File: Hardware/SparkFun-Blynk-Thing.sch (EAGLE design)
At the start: 103 parts, among them IC1 LMV358, Q1 2.5A/30V, Q2 MMBT2222A, Q3 MMBT2222A, U1 MCP73831, U2 ESP8266, U3 AP2112K-3.3V, U4 FT231XS-U, U5 W25Q32FVSS, U6 SI7021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

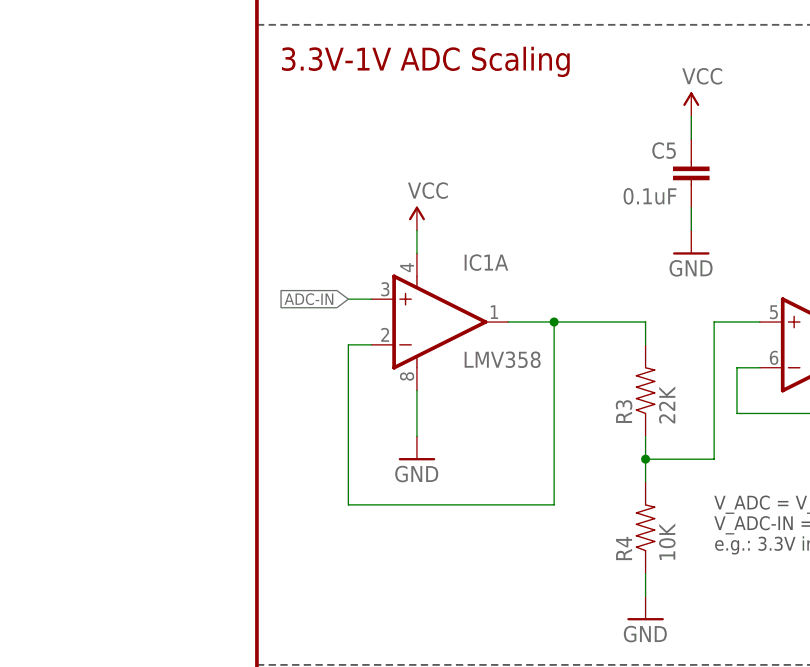
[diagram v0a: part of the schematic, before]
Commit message: Fixing Op amp power supply.
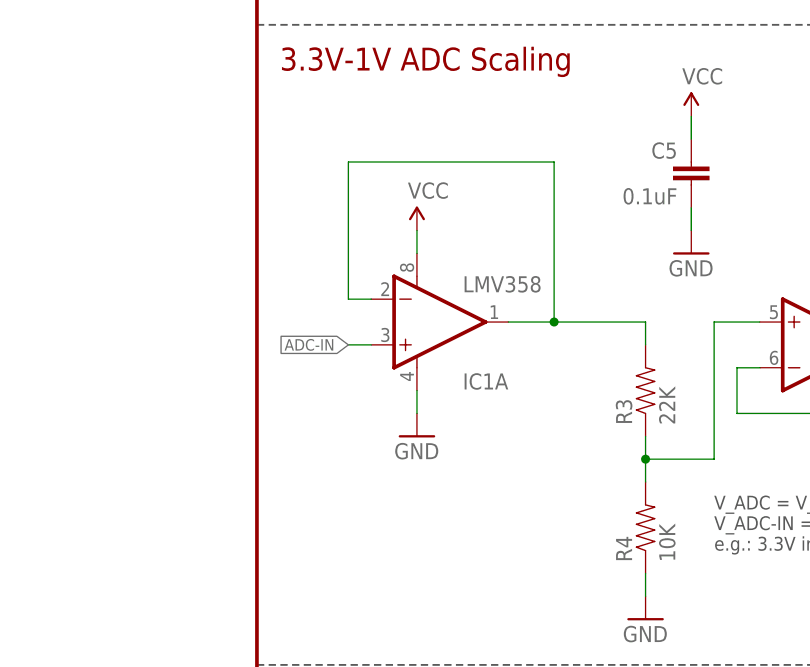
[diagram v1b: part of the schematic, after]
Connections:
- net GND: now also IC1A.V-; no longer IC1A.V+
- net VCC: now also IC1A.V+; no longer IC1A.V-
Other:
- moved on the sheet: IC1A
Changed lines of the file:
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@@
 <part name="R4" library="SparkFun-Resistors" deviceset="10KOHM-1/10W-1%(0603)" device="0603" value="10K"/>
 <part name="GND7" library="SparkFun-Aesthetics" deviceset="GND" device=""/>
-<part name="GND6" library="SparkFun-Aesthetics" deviceset="GND" device=""/>
-<part name="SUPPLY3" library="SparkFun-Aesthetics" deviceset="VCC" device=""/>
 <part name="C5" library="SparkFun-Capacitors" deviceset="0.1UF-25V(+80/-20%)(0603)" device="" value="0.1uF"/>
 <part name="SUPPLY4" library="SparkFun-Aesthetics" deviceset="VCC" device=""/>
@@
 <part name="SUPPLY23" library="SparkFun-Aesthetics" deviceset="V_USB" device=""/>
 <part name="GND41" library="SparkFun-Aesthetics" deviceset="GND" device=""/>
+<part name="SUPPLY1" library="SparkFun-Aesthetics" deviceset="VCC" device=""/>
+<part name="GND6" library="SparkFun-Aesthetics" deviceset="GND" device=""/>
 </parts>
 <sheets>
@@
 <attribute name="VALUE" x="140.716" y="181.356" size="1.778" layer="96" rot="MR0"/>
 </instance>
-<instance part="IC1" gate="A" x="17.78" y="175.26" rot="MR180">
-<attribute name="PROD_ID" x="17.78" y="175.26" size="1.27" layer="96" rot="MR180" display="off"/>
+<instance part="IC1" gate="A" x="17.78" y="175.26">
+<attribute name="PROD_ID" x="17.78" y="175.26" size="1.27" layer="96" display="off"/>
 </instance>
 <instance part="IC1" gate="B" x="63.5" y="172.72"/>
@@
 <instance part="R4" gate="G$1" x="43.18" y="152.4" rot="R90"/>
 <instance part="GND7" gate="1" x="43.18" y="142.24"/>
-<instance part="GND6" gate="1" x="17.78" y="160.02"/>
-<instance part="SUPPLY3" gate="G$1" x="17.78" y="185.42"/>
 <instance part="C5" gate="G$1" x="48.26" y="190.5" rot="MR0"/>
 <instance part="SUPPLY4" gate="G$1" x="48.26" y="198.12"/>
@@
 <instance part="SUPPLY23" gate="G$1" x="231.14" y="256.54" rot="MR0"/>
 <instance part="GND41" gate="1" x="231.14" y="238.76" rot="MR0"/>
+<instance part="SUPPLY1" gate="G$1" x="17.78" y="185.42"/>
+<instance part="GND6" gate="1" x="17.78" y="162.56"/>
 </instances>
 <busses>
@@
 </segment>
 <segment>
-<pinref part="IC1" gate="A" pin="V-"/>
-<pinref part="SUPPLY3" gate="G$1" pin="VCC"/>
-<wire x1="17.78" y1="182.88" x2="17.78" y2="185.42" width="0.1524" layer="91"/>
-</segment>
-<segment>
 <pinref part="C5" gate="G$1" pin="1"/>
 <pinref part="SUPPLY4" gate="G$1" pin="VCC"/>
@@
 <wire x1="416.56" y1="160.02" x2="416.56" y2="170.18" width="0.1524" layer="91"/>
 <pinref part="SUPPLY21" gate="G$1" pin="VCC"/>
+</segment>
+<segment>
+<pinref part="IC1" gate="A" pin="V+"/>
+<pinref part="SUPPLY1" gate="G$1" pin="VCC"/>
+<wire x1="17.78" y1="185.42" x2="17.78" y2="182.88" width="0.1524" layer="91"/>
 </segment>
 </net>
@@
 </segment>
 <segment>
-<pinref part="IC1" gate="A" pin="V+"/>
-<pinref part="GND6" gate="1" pin="GND"/>
-<wire x1="17.78" y1="167.64" x2="17.78" y2="162.56" width="0.1524" layer="91"/>
-</segment>
-<segment>
 <pinref part="C5" gate="G$1" pin="2"/>
 <pinref part="GND8" gate="1" pin="GND"/>
@@
 <pinref part="GND41" gate="1" pin="GND"/>
 <wire x1="231.14" y1="241.3" x2="231.14" y2="243.84" width="0.1524" layer="91"/>
+</segment>
+<segment>
+<pinref part="IC1" gate="A" pin="V-"/>
+<pinref part="GND6" gate="1" pin="GND"/>
+<wire x1="17.78" y1="165.1" x2="17.78" y2="167.64" width="0.1524" layer="91"/>
 </segment>
 </net>
@@
 <wire x1="43.18" y1="175.26" x2="43.18" y2="172.72" width="0.1524" layer="91"/>
 <pinref part="IC1" gate="A" pin="-IN"/>
-<wire x1="12.7" y1="172.72" x2="10.16" y2="172.72" width="0.1524" layer="91"/>
-<wire x1="10.16" y1="172.72" x2="10.16" y2="154.94" width="0.1524" layer="91"/>
-<wire x1="10.16" y1="154.94" x2="33.02" y2="154.94" width="0.1524" layer="91"/>
-<wire x1="33.02" y1="154.94" x2="33.02" y2="175.26" width="0.1524" layer="91"/>
+<wire x1="12.7" y1="177.8" x2="10.16" y2="177.8" width="0.1524" layer="91"/>
+<wire x1="10.16" y1="177.8" x2="10.16" y2="193.04" width="0.1524" layer="91"/>
+<wire x1="10.16" y1="193.04" x2="33.02" y2="193.04" width="0.1524" layer="91"/>
+<wire x1="33.02" y1="193.04" x2="33.02" y2="175.26" width="0.1524" layer="91"/>
 <junction x="33.02" y="175.26"/>
 </segment>
@@
 <segment>
 <pinref part="IC1" gate="A" pin="+IN"/>
-<wire x1="12.7" y1="177.8" x2="10.16" y2="177.8" width="0.1524" layer="91"/>
-<label x="10.16" y="177.8" size="1.27" layer="95" rot="R180" xref="yes"/>
-</segment>
-</net>
+<wire x1="12.7" y1="172.72" x2="10.16" y2="172.72" width="0.1524" layer="91"/>
+<label x="10.16" y="172.72" size="1.27" layer="95" rot="R180" xref="yes"/>
+</segment>
+</net>

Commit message: Fixing Si7021 tCream and tStop.
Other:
- note removed: "- Move WS2812 jumper - Fix Flash package - Fix Op amp power - Fix Si7021 package"
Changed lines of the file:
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@@
 <text x="76.2" y="218.44" size="1.524" layer="97">600mA out
 6V max in</text>
-<text x="-63.5" y="53.34" size="2.54" layer="97">- Move WS2812 jumper
-- Fix Flash package
-- Fix Op amp power
-- Fix Si7021 package</text>
 </plain>
 <instances>

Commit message: Upping version to v02
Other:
- note added: "v02"
- note removed: "v01"
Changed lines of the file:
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@@
 <grid distance="0.1" unitdist="inch" unit="inch" style="lines" multiple="1" display="no" altdistance="0.01" altunitdist="inch" altunit="inch"/>
 <layers>
-<layer number="1" name="Top" color="4" fill="1" visible="yes" active="no"/>
-<layer number="2" name="Route2" color="1" fill="3" visible="yes" active="no"/>
-<layer number="3" name="Route3" color="4" fill="3" visible="yes" active="no"/>
-<layer number="4" name="Route4" color="1" fill="4" visible="yes" active="no"/>
-<layer number="5" name="Route5" color="4" fill="4" visible="yes" active="no"/>
-<layer number="6" name="Route6" color="1" fill="8" visible="yes" active="no"/>
-<layer number="7" name="Route7" color="4" fill="8" visible="yes" active="no"/>
-<layer number="8" name="Route8" color="1" fill="2" visible="yes" active="no"/>
-<layer number="9" name="Route9" color="4" fill="2" visible="yes" active="no"/>
-<layer number="10" name="Route10" color="1" fill="7" visible="yes" active="no"/>
-<layer number="11" name="Route11" color="4" fill="7" visible="yes" active="no"/>
-<layer number="12" name="Route12" color="1" fill="5" visible="yes" active="no"/>
-<layer number="13" name="Route13" color="4" fill="5" visible="yes" active="no"/>
-<layer number="14" name="Route14" color="1" fill="6" visible="yes" active="no"/>
-<layer number="15" name="Route15" color="4" fill="6" visible="yes" active="no"/>
-<layer number="16" name="Bottom" color="1" fill="1" visible="yes" active="no"/>
-<layer number="17" name="Pads" color="2" fill="1" visible="yes" active="no"/>
-<layer number="18" name="Vias" color="2" fill="1" visible="yes" active="no"/>
-<layer number="19" name="Unrouted" color="6" fill="1" visible="yes" active="no"/>
-<layer number="20" name="Dimension" color="15" fill="1" visible="yes" active="no"/>
-<layer number="21" name="tPlace" color="16" fill="1" visible="yes" active="no"/>
-<layer number="22" name="bPlace" color="14" fill="1" visible="yes" active="no"/>
-<layer number="23" name="tOrigins" color="15" fill="1" visible="yes" active="no"/>
-<layer number="24" name="bOrigins" color="15" fill="1" visible="yes" active="no"/>
-<layer number="25" name="tNames" color="7" fill="1" visible="yes" active="no"/>
-<layer number="26" name="bNames" color="7" fill="1" visible="yes" active="no"/>
-<layer number="27" name="tValues" color="7" fill="1" visible="yes" active="no"/>
-<layer number="28" name="bValues" color="7" fill="1" visible="yes" active="no"/>
+<layer number="1" name="Top" color="4" fill="1" visible="no" active="no"/>
+<layer number="2" name="Route2" color="1" fill="3" visible="no" active="no"/>
+<layer number="3" name="Route3" color="4" fill="3" visible="no" active="no"/>
+<layer number="4" name="Route4" color="1" fill="4" visible="no" active="no"/>
+<layer number="5" name="Route5" color="4" fill="4" visible="no" active="no"/>
+<layer number="6" name="Route6" color="1" fill="8" visible="no" active="no"/>
+<layer number="7" name="Route7" color="4" fill="8" visible="no" active="no"/>
+<layer number="8" name="Route8" color="1" fill="2" visible="no" active="no"/>
+<layer number="9" name="Route9" color="4" fill="2" visible="no" active="no"/>
+<layer number="10" name="Route10" color="1" fill="7" visible="no" active="no"/>
+<layer number="11" name="Route11" color="4" fill="7" visible="no" active="no"/>
+<layer number="12" name="Route12" color="1" fill="5" visible="no" active="no"/>
+<layer number="13" name="Route13" color="4" fill="5" visible="no" active="no"/>
+<layer number="14" name="Route14" color="1" fill="6" visible="no" active="no"/>
+<layer number="15" name="Route15" color="4" fill="6" visible="no" active="no"/>
+<layer number="16" name="Bottom" color="1" fill="1" visible="no" active="no"/>
+<layer number="17" name="Pads" color="2" fill="1" visible="no" active="no"/>
+<layer number="18" name="Vias" color="2" fill="1" visible="no" active="no"/>
+<layer number="19" name="Unrouted" color="6" fill="1" visible="no" active="no"/>
+<layer number="20" name="Dimension" color="15" fill="1" visible="no" active="no"/>
+<layer number="21" name="tPlace" color="16" fill="1" visible="no" active="no"/>
+<layer number="22" name="bPlace" color="14" fill="1" visible="no" active="no"/>
+<layer number="23" name="tOrigins" color="15" fill="1" visible="no" active="no"/>
+<layer number="24" name="bOrigins" color="15" fill="1" visible="no" active="no"/>
+<layer number="25" name="tNames" color="7" fill="1" visible="no" active="no"/>
+<layer number="26" name="bNames" color="7" fill="1" visible="no" active="no"/>
+<layer number="27" name="tValues" color="7" fill="1" visible="no" active="no"/>
+<layer number="28" name="bValues" color="7" fill="1" visible="no" active="no"/>
 <layer number="29" name="tStop" color="7" fill="3" visible="no" active="no"/>
 <layer number="30" name="bStop" color="7" fill="6" visible="no" active="no"/>
@@
 <layer number="35" name="tGlue" color="7" fill="4" visible="no" active="no"/>
 <layer number="36" name="bGlue" color="7" fill="5" visible="no" active="no"/>
-<layer number="37" name="tTest" color="7" fill="1" visible="yes" active="no"/>
-<layer number="38" name="bTest" color="7" fill="1" visible="yes" active="no"/>
+<layer number="37" name="tTest" color="7" fill="1" visible="no" active="no"/>
+<layer number="38" name="bTest" color="7" fill="1" visible="no" active="no"/>
 <layer number="39" name="tKeepout" color="4" fill="11" visible="no" active="no"/>
 <layer number="40" name="bKeepout" color="1" fill="11" visible="no" active="no"/>
@@
 <layer number="44" name="Drills" color="7" fill="1" visible="no" active="no"/>
 <layer number="45" name="Holes" color="7" fill="1" visible="no" active="no"/>
-<layer number="46" name="Milling" color="3" fill="1" visible="yes" active="no"/>
-<layer number="47" name="Measures" color="7" fill="1" visible="yes" active="no"/>
-<layer number="48" name="Document" color="7" fill="1" visible="yes" active="no"/>
-<layer number="49" name="Reference" color="7" fill="1" visible="yes" active="no"/>
-<layer number="50" name="dxf" color="7" fill="1" visible="yes" active="no"/>
-<layer number="51" name="tDocu" color="6" fill="1" visible="yes" active="no"/>
-<layer number="52" name="bDocu" color="7" fill="1" visible="yes" active="no"/>
-<layer number="53" name="tGND_GNDA" color="7" fill="9" visible="yes" active="no"/>
-<layer number="54" name="bGND_GNDA" color="1" fill="9" visible="yes" active="no"/>
-<layer number="56" name="wert" color="7" fill="1" visible="yes" active="no"/>
-<layer number="57" name="tCAD" color="7" fill="1" visible="yes" active="no"/>
-<layer number="59" name="tCarbon" color="7" fill="1" visible="yes" active="no"/>
-<layer number="60" name="bCarbon" color="7" fill="1" visible="yes" active="no"/>
+<layer number="46" name="Milling" color="3" fill="1" visible="no" active="no"/>
+<layer number="47" name="Measures" color="7" fill="1" visible="no" active="no"/>
+<layer number="48" name="Document" color="7" fill="1" visible="no" active="no"/>
+<layer number="49" name="Reference" color="7" fill="1" visible="no" active="no"/>
+<layer number="50" name="dxf" color="7" fill="1" visible="no" active="no"/>
+<layer number="51" name="tDocu" color="6" fill="1" visible="no" active="no"/>
+<layer number="52" name="bDocu" color="7" fill="1" visible="no" active="no"/>
+<layer number="53" name="tGND_GNDA" color="7" fill="9" visible="no" active="no"/>
+<layer number="54" name="bGND_GNDA" color="1" fill="9" visible="no" active="no"/>
+<layer number="56" name="wert" color="7" fill="1" visible="no" active="no"/>
+<layer number="57" name="tCAD" color="7" fill="1" visible="no" active="no"/>
+<layer number="59" name="tCarbon" color="7" fill="1" visible="no" active="no"/>
+<layer number="60" name="bCarbon" color="7" fill="1" visible="no" active="no"/>
 <layer number="90" name="Modules" color="5" fill="1" visible="yes" active="yes"/>
 <layer number="91" name="Nets" color="2" fill="1" visible="yes" active="yes"/>
@@
 lots of power.)</text>
 <text x="355.346" y="11.43" size="2.54" layer="94" rot="MR180" align="top-left">Jim Lindblom</text>
-<text x="421.64" y="10.16" size="2.54" layer="94" align="top-left">v01</text>
+<text x="421.64" y="10.16" size="2.54" layer="94" align="top-left">v02</text>
 <text x="332.486" y="6.35" size="2.032" layer="97" rot="MR180" align="top-left">Auto-reset circuit based on NodeMCU Dev Kit</text>
 <text x="386.08" y="76.2" size="1.524" layer="97">GPIO2 pulled up in I2C section</text>
